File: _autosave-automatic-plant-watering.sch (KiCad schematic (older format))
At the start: 43 parts, among them J2 USB_B_Mini, J3 MOTOR, J4 INPUT, J5 Power, Q1 BC847, Q2 BC847, Q3 TEPT4400, SW1 SW_Push, U1 ESP32-WROOM-32D, U3 USBLC6-2SC6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

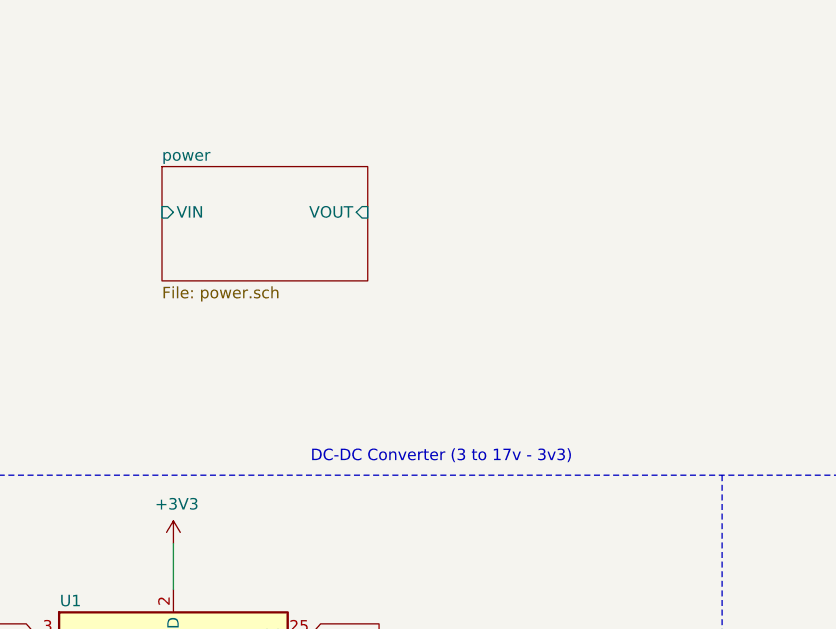
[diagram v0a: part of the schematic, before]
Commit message: removing USB to UART
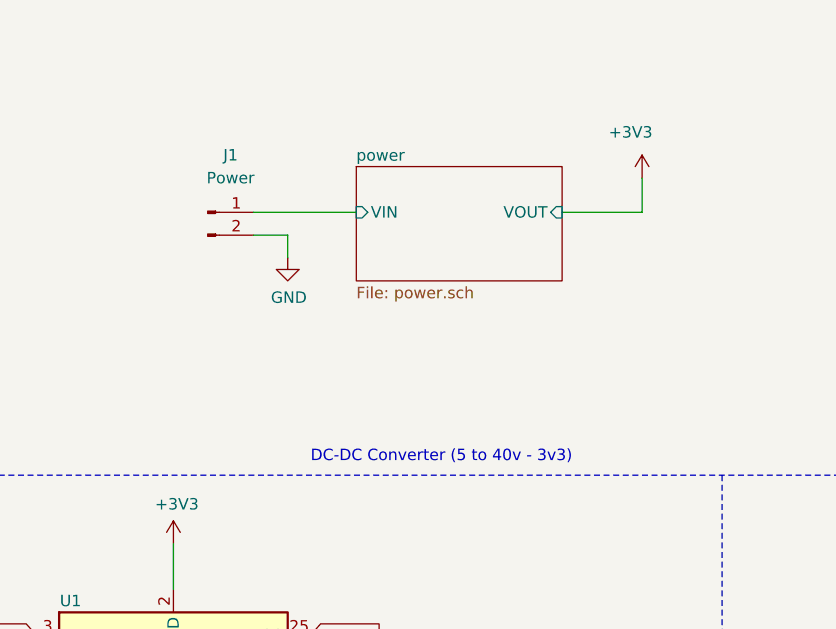
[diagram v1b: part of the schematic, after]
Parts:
- added J1: Power, Connector_Molex:Molex_KK-254_AE-6410-02A_1x02_P2.54mm_Vertical, symbol Connector:Conn_01x02_Male
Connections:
- net GND: now also J1.2 (Pin_2)
- net power/VIN: now also J1.1 (Pin_1)
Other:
- note added: "DC-DC Converter (5 to 40v - 3v3)\n"
- note removed: "DC-DC Converter (3 to 17v - 3v3)\n"
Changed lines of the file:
@@
 	3150 3900 3150 3850
 Text Notes 2150 2400 0    50   ~ 0
-DC-DC Converter (3 to 17v - 3v3)\n
+DC-DC Converter (5 to 40v - 3v3)\n
 Text Notes 4550 5800 0    50   ~ 0
 Programming Switches\n
@@
 	3550 3900 3550 3850
 $Sheet
-S 1500 1100 900  500
+S 2350 1100 900  500
 U 62D8A179
 F0 "power" 50
 F1 "power.sch" 50
-F2 "VOUT" I R 2400 1300 50
-F3 "VIN" I L 1500 1300 50
+F2 "VOUT" I R 3250 1300 50
+F3 "VIN" I L 2350 1300 50
 $EndSheet
+$Comp
+L power:+3V3 #PWR0118
+U 1 1 62E5CC95
+P 3600 1150
+F 0 "#PWR0118" H 3600 1000 50  0001 C CNN
+F 1 "+3V3" H 3550 1350 50  0000 C CNN
+F 2 "" H 3600 1150 50  0001 C CNN
+F 3 "" H 3600 1150 50  0001 C CNN
+	1    3600 1150
+	1    0    0    -1
+$EndComp
+Wire Wire Line
+	3600 1300 3600 1150
+Wire Wire Line
+	3250 1300 3600 1300
+$Comp
+L Connector:Conn_01x02_Male J1
+U 1 1 62E6B4A5
+P 1700 1300
+F 0 "J1" H 1800 1550 50  0000 C CNN
+F 1 "Power" H 1800 1450 50  0000 C CNN
+F 2 "Connector_Molex:Molex_KK-254_AE-6410-02A_1x02_P2.54mm_Vertical" H 1700 1300 50  0001 C CNN
+F 3 "~" H 1700 1300 50  0001 C CNN
+	1    1700 1300
+	1    0    0    -1
+$EndComp
+Wire Wire Line
+	1900 1300 2350 1300
+$Comp
+L power:GND #PWR0119
+U 1 1 62E73873
+P 2050 1500
+F 0 "#PWR0119" H 2050 1250 50  0001 C CNN
+F 1 "GND" H 2055 1327 50  0000 C CNN
+F 2 "" H 2050 1500 50  0001 C CNN
+F 3 "" H 2050 1500 50  0001 C CNN
+	1    2050 1500
+	1    0    0    -1
+$EndComp
+Wire Wire Line
+	2050 1400 1900 1400
+Wire Wire Line
+	2050 1400 2050 1500
 $EndSCHEMATC
